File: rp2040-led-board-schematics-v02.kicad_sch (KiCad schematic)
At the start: 47 parts, among them J27 MainBoard, J5 PWR_IN, J9 FrontPanel, SW1 PEC16, SW2 Button, U1 Pico, U5 LM7805, U6 ENC28J60

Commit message: fix power sources, update reveivers accordingly (main board PCB not updated yet)
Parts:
- removed C14: 220nF, Capacitor_SMD:C_0603_1608Metric, symbol Device:C_Small
- removed C15: 100nF, Capacitor_SMD:C_0603_1608Metric, symbol Device:C_Small
- removed JP5: 12V, Jumper:SolderJumper-2_P1.3mm_Open_Pad1.0x1.5mm, symbol Jumper:SolderJumper_2_Open
- removed U5: LM7805, Package_TO_SOT_SMD:SOT-223, symbol Regulator_Linear:LM7805_TO220
- added C11: 1uF, Capacitor_SMD:C_0603_1608Metric, symbol Device:C_Small
- added C71: 100nF, Capacitor_SMD:C_0603_1608Metric, symbol Device:C_Small
- added C72: 100nF, Capacitor_SMD:C_0402_1005Metric, symbol Device:C_Small
- added C74: 10uF, Capacitor_SMD:C_1206_3216Metric, symbol Device:C_Small
- added F1: 1A, symbol Device:Polyfuse_Small
- added FB2: 600 @ 600Mhz, symbol Device:FerriteBead_Small
- added JP19: 12V, Jumper:SolderJumper-2_P1.3mm_Open_Pad1.0x1.5mm, symbol Jumper:SolderJumper_2_Open
- added L1: 5.6mH 120mOhm, symbol Device:L_Small
- added Q1: AO3401A, Package_TO_SOT_SMD:SOT-23, symbol Transistor_FET:AO3401A
- added U2: LMR50410Y5FQDBVRQ1, Package_TO_SOT_SMD:SOT-23-6, symbol Library:LMR50410Y5FQDBVRQ1
- C33, C34, C35, C36: LCSC Part # C1525 -> (none); LCSC Part Number C1525 -> (none)
- R52, R53, R54, R55, R56, R57, R58, R59: LCSC Part # C4328 -> (none); LCSC Part Number C4328 -> (none)
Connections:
- net +12V: now also F1.1
- net +5V: now also JP19.2 (B)
- net GND: now also C11.2, C71.2, C74.2, Q1.1 (G), U2.2 (GND)
- new net: FB2.1, Q1.2 (S)
- new net: C72.2, U2.1 (CB)
- new net: C72.1, L1.1, U2.6 (SW)
- new net: F1.2, Q1.3 (D)
- new net Buck in: C11.1, C71.1, FB2.2, U2.4 (EN), U2.5 (VIN)
- new net Buck out: C74.1, JP19.1 (A), L1.2, U2.3 (FB)
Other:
- note added: "current draw: ~400mA"
- note added: "current output: 1A max"
- note added: "total current draw: ~750mA"
- note removed: "current draw: ~200mA (sure ?)"
- note removed: "current output: ~1A"
- note removed: "total current draw: ~400mA"
- moved on the sheet: H1, H10, H11, H22, H23, H25, H26, H3, H4, J5, JP10

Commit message: should be ready to find parts
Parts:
- F1: footprint (none) -> Fuse:Fuse_1206_3216Metric
- FB2: footprint (none) -> Inductor_SMD:L_0805_2012Metric
- L1: footprint (none) -> Inductor_SMD:L_Sunlord_MWSA0503S
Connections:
- net SW: now reaches C72.1, L1.1, U2.6 (SW)
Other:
- moved on the sheet: FM1, FM2, FM3, FM4, H1, H2, H32, H33

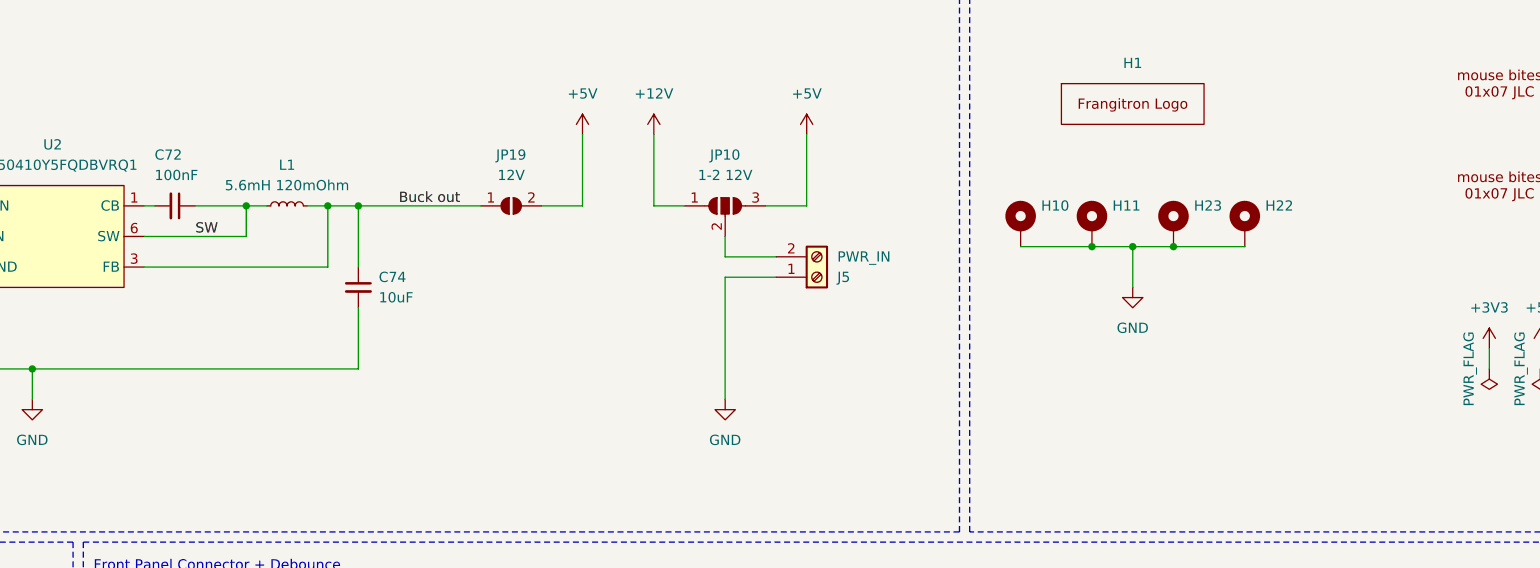
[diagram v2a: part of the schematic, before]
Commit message: fix: DRC & ERC revealed designators were out of sync between schem and pcb
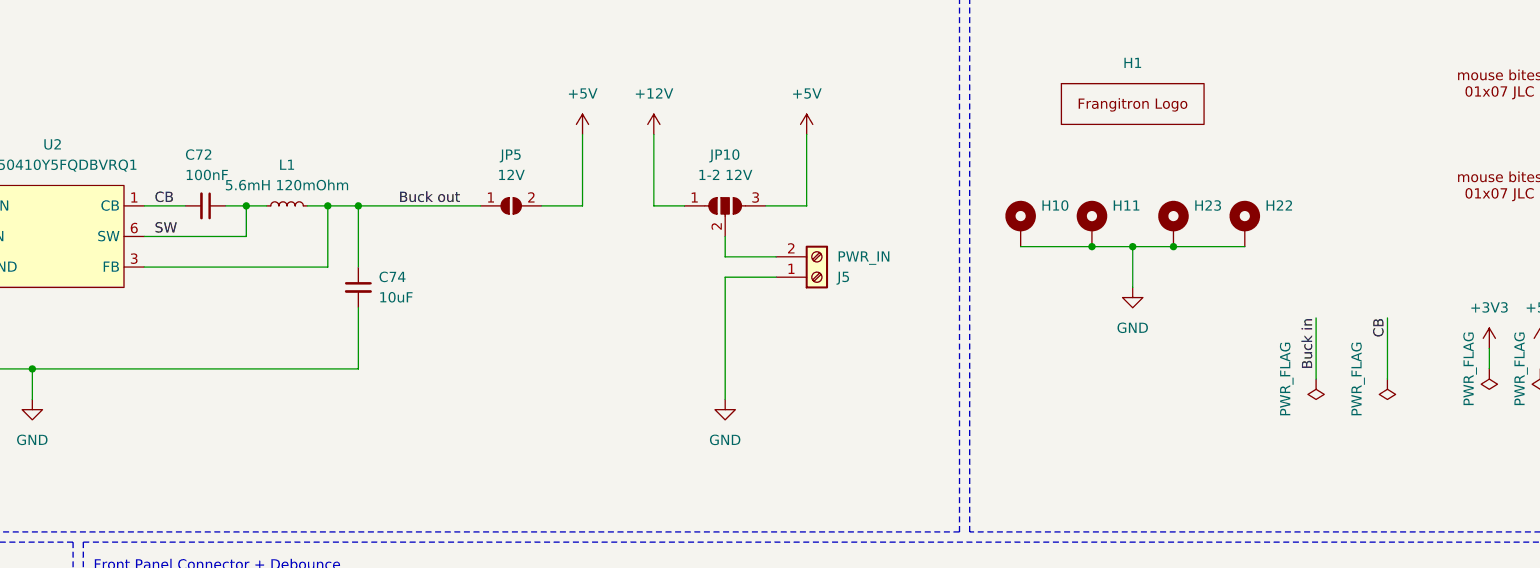
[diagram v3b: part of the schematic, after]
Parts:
- renumbered JP19 to JP5
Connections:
- net CB: now reaches C72.2, U2.1 (CB)
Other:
- moved on the sheet: C72
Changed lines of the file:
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@@
     (stroke (width 0) (type default))
   )
+  (wire (pts (xy 463.55 87.63) (xy 463.55 95.25))
+    (stroke (width 0) (type default))
+  )
   (wire (pts (xy 147.32 99.06) (xy 149.86 99.06))
     (stroke (width 0) (type default))
@@
     (stroke (width 0) (type default))
   )
-  (wire (pts (xy 314.96 73.66) (xy 321.31 73.66))
+  (wire (pts (xy 318.77 73.66) (xy 321.31 73.66))
     (stroke (width 0) (type default))
   )
@@
     (stroke (width 0) (type default))
   )
+  (wire (pts (xy 454.66 87.63) (xy 454.66 95.25))
+    (stroke (width 0) (type default))
+  )
   (wire (pts (xy 335.28 73.66) (xy 335.28 81.28))
     (stroke (width 0) (type default))
@@
     (stroke (width 0) (type default))
   )
-  (wire (pts (xy 308.61 73.66) (xy 309.88 73.66))
+  (wire (pts (xy 308.61 73.66) (xy 313.69 73.66))
     (stroke (width 0) (type default))
   )
@@
     (effects (font (size 1.27 1.27)) (justify left bottom))
   )
-  (label "SW" (at 314.96 77.47 0) (fields_autoplaced)
+  (label "SW" (at 309.88 77.47 0) (fields_autoplaced)
     (effects (font (size 1.27 1.27)) (justify left bottom))
   )
@@
     (effects (font (size 1.27 1.27)) (justify left bottom))
   )
+  (label "CB" (at 309.88 73.66 0) (fields_autoplaced)
+    (effects (font (size 1.27 1.27)) (justify left bottom))
+  )
   (label "FP GND" (at 193.04 267.97 0) (fields_autoplaced)
     (effects (font (size 1.27 1.27)) (justify left bottom))
   )
+  (label "Buck in" (at 454.66 87.63 270) (fields_autoplaced)
+    (effects (font (size 1.27 1.27)) (justify right bottom))
+  )
   (label "FP GND" (at 86.36 267.97 0) (fields_autoplaced)
     (effects (font (size 1.27 1.27)) (justify left bottom))
@@
     (effects (font (size 1.27 1.27)) (justify left bottom))
   )
+  (label "CB" (at 463.55 87.63 270) (fields_autoplaced)
+    (effects (font (size 1.27 1.27)) (justify right bottom))
+  )
   (label "FP +3V3" (at 260.35 248.92 0) (fields_autoplaced)
     (effects (font (size 1.27 1.27)) (justify left bottom))
@@
     )
   )
+  (symbol (lib_id "power:PWR_FLAG") (at 454.66 95.25 0) (mirror x) (unit 1)
+    (in_bom yes) (on_board yes) (dnp no)
+    (property "Reference" "#FLG034" (at 454.66 97.155 0)
+      (effects (font (size 1.27 1.27)) hide)
+    )
+    (property "Value" "PWR_FLAG" (at 450.85 95.25 90)
+      (effects (font (size 1.27 1.27)))
+    )
+    (property "Footprint" "" (at 454.66 95.25 0)
+      (effects (font (size 1.27 1.27)) hide)
+    )
+    (property "Datasheet" "~" (at 454.66 95.25 0)
+      (effects (font (size 1.27 1.27)) hide)
+    )
+    (pin "1")
+    (instances
+      (project "rp2040-led-board-schematics-v02"
+        (path "/c1a38541-3f06-4b3b-ba3a-decae3ac3c31"
+          (reference "#FLG034") (unit 1)
+        )
+      )
+    )
+  )
   (symbol (lib_id "power:GND") (at 439.42 172.72 0) (mirror y) (unit 1)
     (in_bom yes) (on_board yes) (dnp no) (fields_autoplaced)
@@
     )
   )
+  (symbol (lib_id "power:PWR_FLAG") (at 463.55 95.25 0) (mirror x) (unit 1)
+    (in_bom yes) (on_board yes) (dnp no)
+    (property "Reference" "#FLG033" (at 463.55 97.155 0)
+      (effects (font (size 1.27 1.27)) hide)
+    )
+    (property "Value" "PWR_FLAG" (at 459.74 95.25 90)
+      (effects (font (size 1.27 1.27)))
+    )
+    (property "Footprint" "" (at 463.55 95.25 0)
+      (effects (font (size 1.27 1.27)) hide)
+    )
+    (property "Datasheet" "~" (at 463.55 95.25 0)
+      (effects (font (size 1.27 1.27)) hide)
+    )
+    (pin "1")
+    (instances
+      (project "rp2040-led-board-schematics-v02"
+        (path "/c1a38541-3f06-4b3b-ba3a-decae3ac3c31"
+          (reference "#FLG033") (unit 1)
+        )
+      )
+    )
+  )
   (symbol (lib_id "Device:R_Small") (at 330.2 152.4 270) (unit 1)
     (in_bom yes) (on_board yes) (dnp no)
@@
   (symbol (lib_id "Jumper:SolderJumper_2_Open") (at 354.33 73.66 0) (unit 1)
     (in_bom yes) (on_board yes) (dnp no) (fields_autoplaced)
-    (property "Reference" "JP19" (at 354.33 67.31 0)
+    (property "Reference" "JP5" (at 354.33 67.31 0)
       (effects (font (size 1.27 1.27)))
     )
@@
       (project "rp2040-led-board-schematics-v02"
         (path "/c1a38541-3f06-4b3b-ba3a-decae3ac3c31"
-          (reference "JP19") (unit 1)
+          (reference "JP5") (unit 1)
         )
       )
@@
     )
   )
-  (symbol (lib_id "Device:C_Small") (at 312.42 73.66 270) (mirror x) (unit 1)
+  (symbol (lib_id "Device:C_Small") (at 316.23 73.66 270) (mirror x) (unit 1)
     (in_bom yes) (on_board yes) (dnp no)
-    (property "Reference" "C72" (at 309.88 67.31 90)
+    (property "Reference" "C72" (at 313.69 67.31 90)
       (effects (font (size 1.27 1.27)) (justify left))
     )
-    (property "Value" "100nF" (at 309.88 69.85 90)
+    (property "Value" "100nF" (at 313.69 69.85 90)
       (effects (font (size 1.27 1.27)) (justify left))
     )
-    (property "Footprint" "Capacitor_SMD:C_0402_1005Metric" (at 312.42 73.66 0)
+    (property "Footprint" "Capacitor_SMD:C_0402_1005Metric" (at 316.23 73.66 0)
       (effects (font (size 1.27 1.27)) hide)
     )
-    (property "Datasheet" "~" (at 312.42 73.66 0)
+    (property "Datasheet" "~" (at 316.23 73.66 0)
       (effects (font (size 1.27 1.27)) hide)
     )
-    (property "LCSC Part Number" "" (at 312.42 73.66 0)
+    (property "LCSC Part Number" "" (at 316.23 73.66 0)
       (effects (font (size 1.27 1.27)) hide)
     )
-    (property "LCSC Part #" "" (at 312.42 73.66 0)
+    (property "LCSC Part #" "" (at 316.23 73.66 0)
       (effects (font (size 1.27 1.27)) hide)
     )
-    (property "URL" "" (at 312.42 73.66 0)
+    (property "URL" "" (at 316.23 73.66 0)
       (effects (font (size 1.27 1.27)) hide)
     )

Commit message: order placed
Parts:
- L1: value 5.6mH 120mOhm -> 5.6mH
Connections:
- net +12V: now also FB2.1; no longer F1.1
- net at Q1.2 (S): now also F1.2; no longer FB2.1
- net at J5.2 (Pin_2): now also Q1.3 (D); no longer JP10.2 (C)
- new net: F1.1, JP10.2 (C)
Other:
- note added: "120 Ohm"
- note added: "measured current draw for one dev card : 5.3 mA"
- note added: "total current draw: ~750mA measured current draw at prototype: ~300mA"
- note removed: "total current draw: ~750mA"
- moved on the sheet: C11, C71, C72, C74, FB2, J5, JP10, JP5, L1, U2
